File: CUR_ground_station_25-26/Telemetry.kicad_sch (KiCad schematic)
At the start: 0 parts

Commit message: added buncha stuff from flight computer
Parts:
- added C6: 1u, Capacitor_SMD:C_0603_1608Metric, symbol Device:C_Small
- added C8, C9: C_Small, Capacitor_SMD:C_0603_1608Metric, symbol Device:C_Small
- added J3: Conn_Coaxial_Small, Connector_Coxaial_RFSOLUTIONS_CON-SMA-EDGE-S:Conn_Coaxial_RFSOLUTIONS_CON-SMA-EDGE-S, symbol Connector:Conn_Coaxial_Small
- added R23: 10k, Resistor_SMD:R_0603_1608Metric, symbol Device:R_Small_US
- added R24, R25: 0, Resistor_SMD:R_0603_1608Metric, symbol Device:R_Small_US
- added TP1, TP10, TP11, TP2, TP3, TP4, TP5, TP6, TP7, TP8, TP9: TestPoint_Small, TestPoint_KOASpeer:TestPoint_Chip_RCUCTE_0603, symbol Connector:TestPoint_Small
- added U5: E22-400MM_22S, EBYTE_LoRa:EBYTE_LoRA_E22-400MM22S, symbol EBYTE_LoRa:EBYTE_LoRa_E22-400MM22S
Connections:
- new net: C9.1, J3.1 (In), R25.1
- new net: C8.1, R25.2, U5.6 (ANT)
- new net +3V3: C6.1, R23.1, U5.1 (VCC)
- new net GND: C6.2, C8.2, C9.2, J3.2 (Ext), U5.16 (GND), U5.2 (GND), U5.7 (GND)
- new net RF_BUSY: TP3.1, U5.11 (BUSY)
- new net RF_IO1: TP9.1, U5.18 (DIO1)
- new net RF_IO2: R24.2, TP10.1, U5.19 (DIO2)
- new net RF_IO3: TP11.1, U5.20 (DIO3)
- new net RF_MISO: TP7.1, U5.12 (MISO)
- new net RF_MOSI: TP1.1, U5.13 (MOSI)
- new net RF_RXEN: TP4.1, U5.10 (RXEN)
- new net RF_SCK: TP2.1, U5.15 (SCK)
- new net RF_TXEN: R24.1, TP5.1, U5.9 (TXEN)
- new net ~{RF_NSS}: R23.2, TP8.1, U5.14 (NSS)
- new net ~{RF_RESET}: TP6.1, U5.3 (NRST)
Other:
- note added: "DIO1 - interrupt DIO2 - tx switch"
- note added: "Just in case something weird is happening here"
- note added: "Pick capacitor values to PI match antenna - leave to test later - do not place in BOM"
- note added: "RF Module"

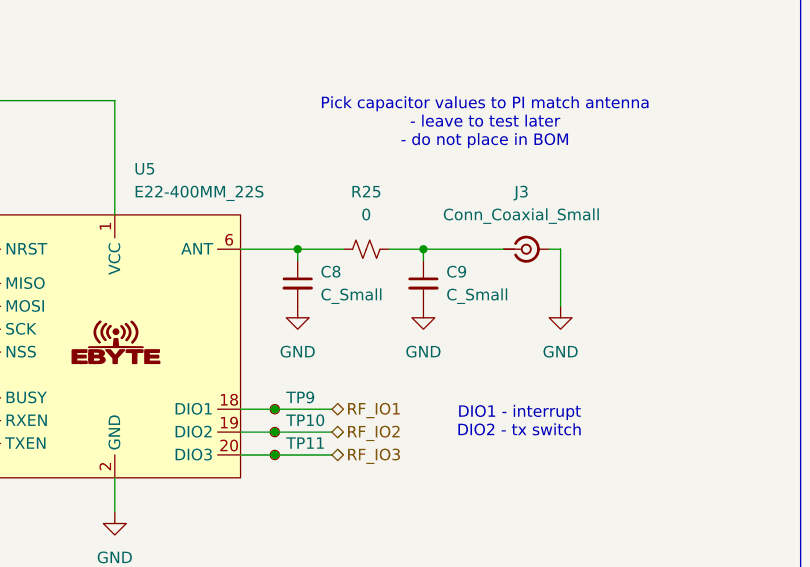
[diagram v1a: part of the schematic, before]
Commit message: DNP the tuning capacitors on the RF trace
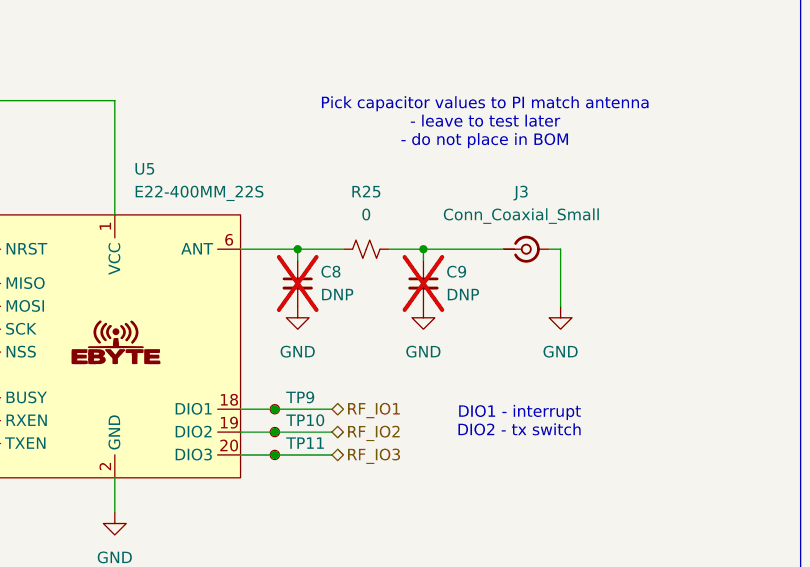
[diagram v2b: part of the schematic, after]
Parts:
- C8, C9: value C_Small -> DNP; now not fitted
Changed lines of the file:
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@@
 		(in_bom yes)
 		(on_board yes)
-		(dnp no)
+		(dnp yes)
 		(fields_autoplaced yes)
 		(property "Reference" "C8"
@@
 			)
 		)
-		(property "Value" "C_Small"
+		(property "Value" "DNP"
 			(at 106.68 60.9662 0)
 			(effects
@@
 		(in_bom yes)
 		(on_board yes)
-		(dnp no)
+		(dnp yes)
 		(fields_autoplaced yes)
 		(property "Reference" "C9"
@@
 			)
 		)
-		(property "Value" "C_Small"
+		(property "Value" "DNP"
 			(at 120.65 60.9662 0)
 			(effects

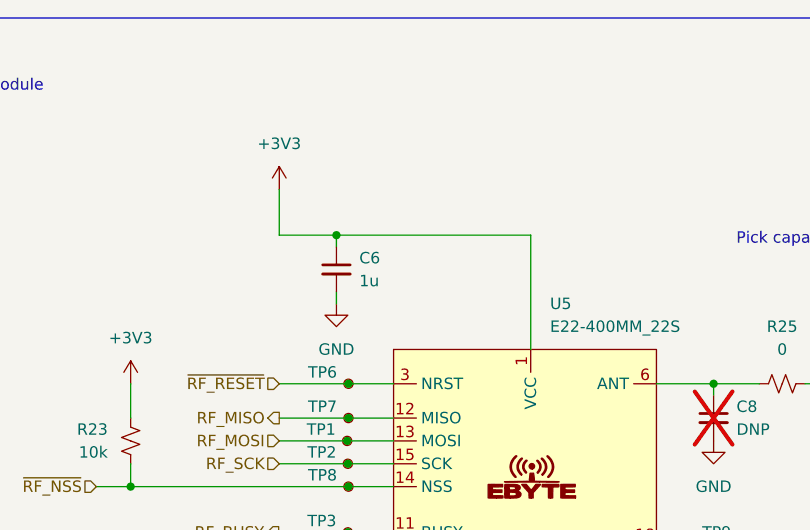
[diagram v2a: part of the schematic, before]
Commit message: Add some required MCU components
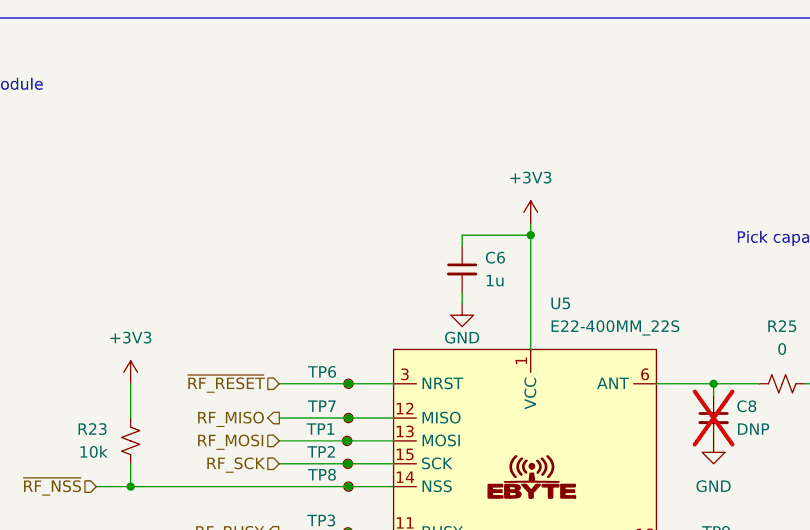
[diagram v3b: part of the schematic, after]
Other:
- moved on the sheet: C6
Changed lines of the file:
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@@
-	)
-	(junction
-		(at 62.23 39.37)
-		(diameter 0)
-		(color 0 0 0 0)
 	)
 	(junction
@@
 	)
 	(junction
+		(at 83.82 39.37)
+		(diameter 0)
+		(color 0 0 0 0)
+	)
+	(junction
 		(at 39.37 67.31)
 		(diameter 0)
@@
 	(wire
 		(pts
-			(xy 62.23 40.64) (xy 62.23 39.37)
+			(xy 76.2 40.64) (xy 76.2 39.37)
 		)
 		(stroke
@@
 	(wire
 		(pts
-			(xy 55.88 34.29) (xy 55.88 39.37)
+			(xy 83.82 38.1) (xy 83.82 39.37)
 		)
 		(stroke
@@
 	(wire
 		(pts
-			(xy 62.23 39.37) (xy 83.82 39.37)
+			(xy 76.2 39.37) (xy 83.82 39.37)
 		)
 		(stroke
@@
 	(wire
 		(pts
-			(xy 62.23 45.72) (xy 62.23 46.99)
+			(xy 76.2 45.72) (xy 76.2 46.99)
 		)
 		(stroke
@@
 		(pts
 			(xy 39.37 55.88) (xy 39.37 59.69)
-		)
-		(stroke
-			(width 0)
-			(type default)
-		)
-	)
-	(wire
-		(pts
-			(xy 55.88 39.37) (xy 62.23 39.37)
 		)
 		(stroke
@@
 	(symbol
 		(lib_id "power:GND")
-		(at 62.23 46.99 0)
+		(at 76.2 46.99 0)
 		(mirror y)
 		(unit 1)
@@
 		(on_board yes)
 		(dnp no)
-		(fields_autoplaced yes)
 		(property "Reference" "#PWR036"
-			(at 62.23 53.34 0)
+			(at 76.2 53.34 0)
 			(effects
 				(font
@@
 		)
 		(property "Value" "GND"
-			(at 62.23 52.07 0)
+			(at 76.2 50.8 0)
 			(effects
 				(font
@@
 		)
 		(property "Footprint" ""
-			(at 62.23 46.99 0)
+			(at 76.2 46.99 0)
 			(effects
 				(font
@@
 		)
 		(property "Datasheet" ""
-			(at 62.23 46.99 0)
+			(at 76.2 46.99 0)
 			(effects
 				(font
@@
 		)
 		(property "Description" "Power symbol creates a global label with name \"GND\" , ground"
-			(at 62.23 46.99 0)
+			(at 76.2 46.99 0)
 			(effects
 				(font
@@
 	(symbol
 		(lib_id "Device:C_Small")
-		(at 62.23 43.18 0)
+		(at 76.2 43.18 0)
 		(mirror y)
 		(unit 1)
@@
 		(fields_autoplaced yes)
 		(property "Reference" "C6"
-			(at 64.77 41.9162 0)
+			(at 78.74 41.9162 0)
 			(effects
 				(font
@@
 		)
 		(property "Value" "1u"
-			(at 64.77 44.4562 0)
+			(at 78.74 44.4562 0)
 			(effects
 				(font
@@
 		)
 		(property "Footprint" "Capacitor_SMD:C_0603_1608Metric"
-			(at 62.23 43.18 0)
+			(at 76.2 43.18 0)
 			(effects
 				(font
@@
 		)
 		(property "Datasheet" "~"
-			(at 62.23 43.18 0)
+			(at 76.2 43.18 0)
 			(effects
 				(font
@@
 		)
 		(property "Description" "Unpolarized capacitor, small symbol"
-			(at 62.23 43.18 0)
+			(at 76.2 43.18 0)
 			(effects
 				(font
@@
 	(symbol
 		(lib_id "power:+3V3")
-		(at 55.88 34.29 0)
+		(at 83.82 38.1 0)
 		(unit 1)
 		(exclude_from_sim no)
@@
 		(fields_autoplaced yes)
 		(property "Reference" "#PWR035"
-			(at 55.88 38.1 0)
+			(at 83.82 41.91 0)
 			(effects
 				(font
@@
 		)
 		(property "Value" "+3V3"
-			(at 55.88 29.21 0)
+			(at 83.82 33.02 0)
 			(effects
 				(font
@@
 		)
 		(property "Footprint" ""
-			(at 55.88 34.29 0)
+			(at 83.82 38.1 0)
 			(effects
 				(font
@@
 		)
 		(property "Datasheet" ""
-			(at 55.88 34.29 0)
+			(at 83.82 38.1 0)
 			(effects
 				(font
@@
 		)
 		(property "Description" "Power symbol creates a global label with name \"+3V3\""
-			(at 55.88 34.29 0)
-			(effects
-				(font
+			(at 83.82 38.1 0)
+			(effects
+				(font

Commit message: added more footprints
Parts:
- J3: footprint Connector_Coxaial_RFSOLUTIONS_CON-SMA-EDGE-S:Conn_Coaxial_RFSOLUTIONS_CON-SMA-EDGE-S -> Conn_Coaxial_RFSOLUTIONS_CON-SMA-EDGE-S:Conn_Coaxial_RFSOLUTIONS_CON-SMA-EDGE-S
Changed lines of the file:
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@@
 			)
 		)
-		(property "Footprint" "Connector_Coxaial_RFSOLUTIONS_CON-SMA-EDGE-S:Conn_Coaxial_RFSOLUTIONS_CON-SMA-EDGE-S"
+		(property "Footprint" "Conn_Coaxial_RFSOLUTIONS_CON-SMA-EDGE-S:Conn_Coaxial_RFSOLUTIONS_CON-SMA-EDGE-S"
 			(at 129.54 55.88 0)
 			(effects

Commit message: BOM optimization
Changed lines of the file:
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@@
 		(lib_id "Device:R_Small_US")
 		(at 62.23 82.55 0)
+		(mirror y)
 		(unit 1)
 		(exclude_from_sim no)
@@
 		(dnp no)
 		(property "Reference" "R24"
-			(at 64.7429 81.2799 0)
+			(at 59.7171 81.2799 0)
 			(effects
 				(font
@@
 		)
 		(property "Value" "0"
-			(at 64.7429 85.0899 0)
+			(at 59.7171 85.0899 0)
 			(effects
 				(font

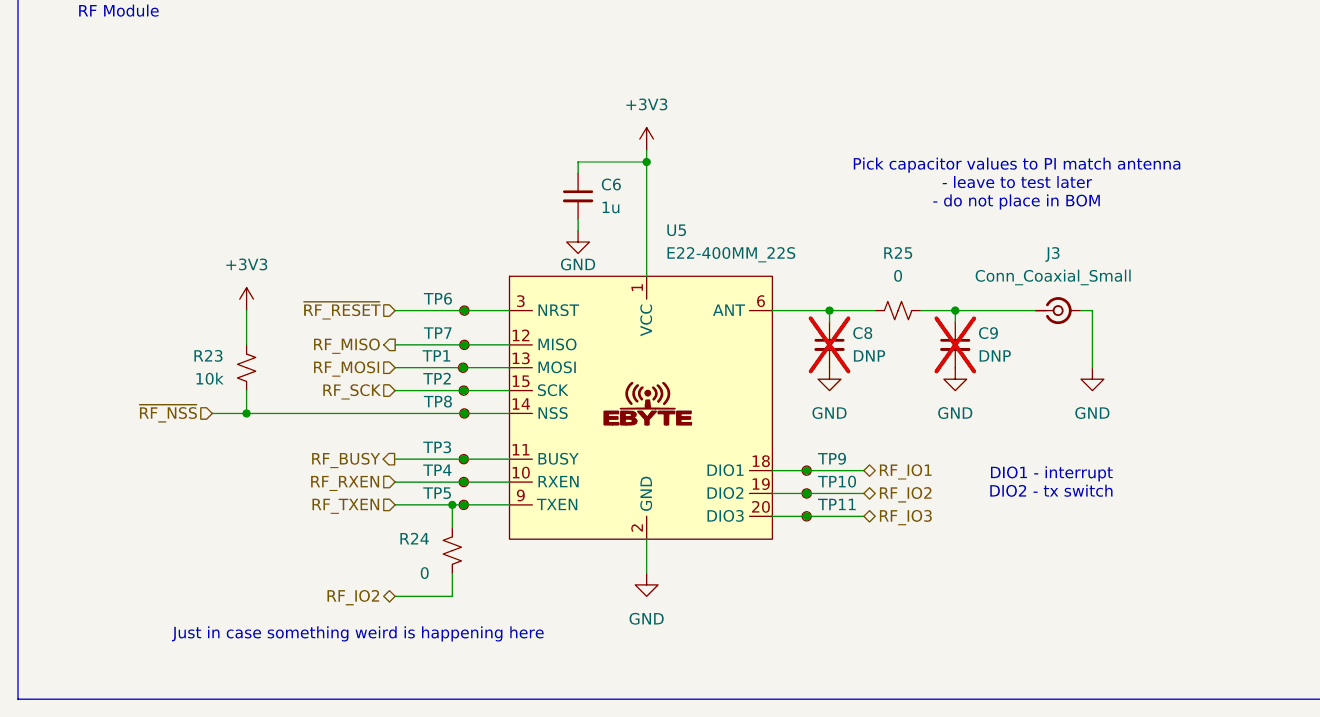
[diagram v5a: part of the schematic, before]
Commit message: Fix library issues in board update
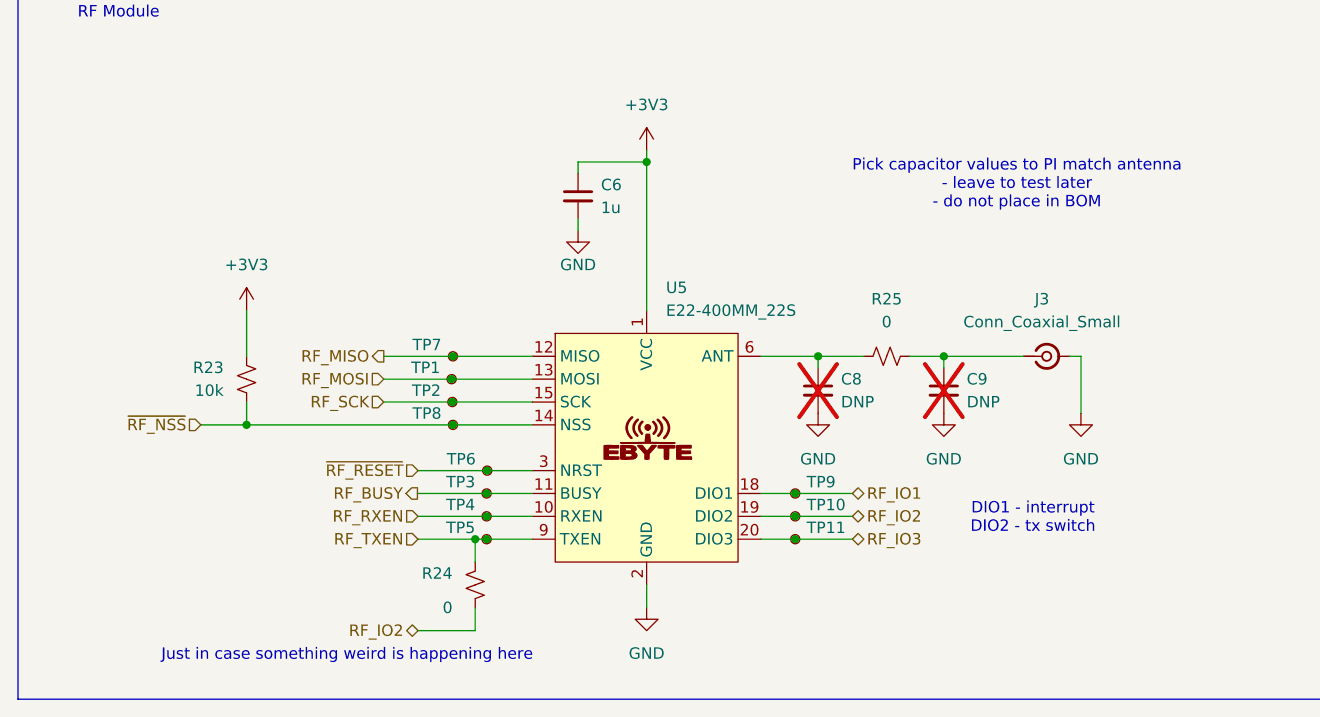
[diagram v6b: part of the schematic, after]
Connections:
- new net: U5.17 (NC), U5.4 (NC), U5.5 (NC), U5.8 (NC)
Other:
- moved on the sheet: C8, C9, J3, R23, R24, R25, TP1, TP10, TP11, TP2, TP3, TP4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

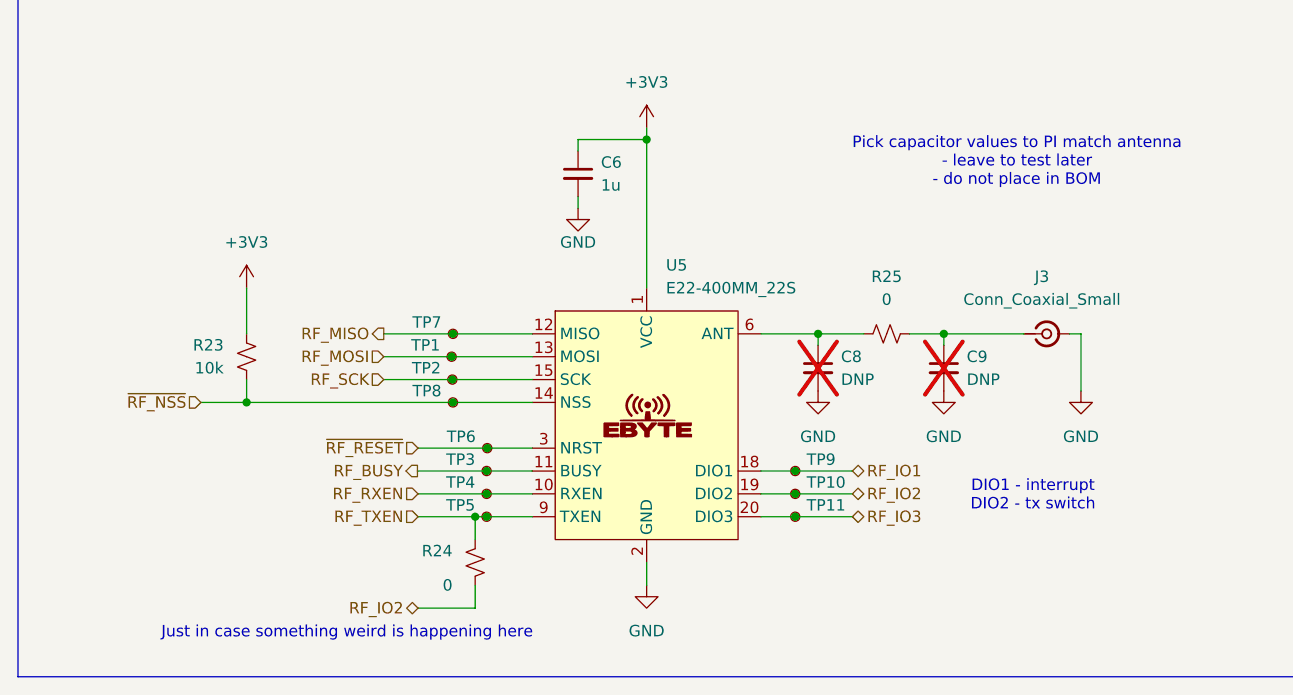
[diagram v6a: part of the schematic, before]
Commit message: Find MPNs again
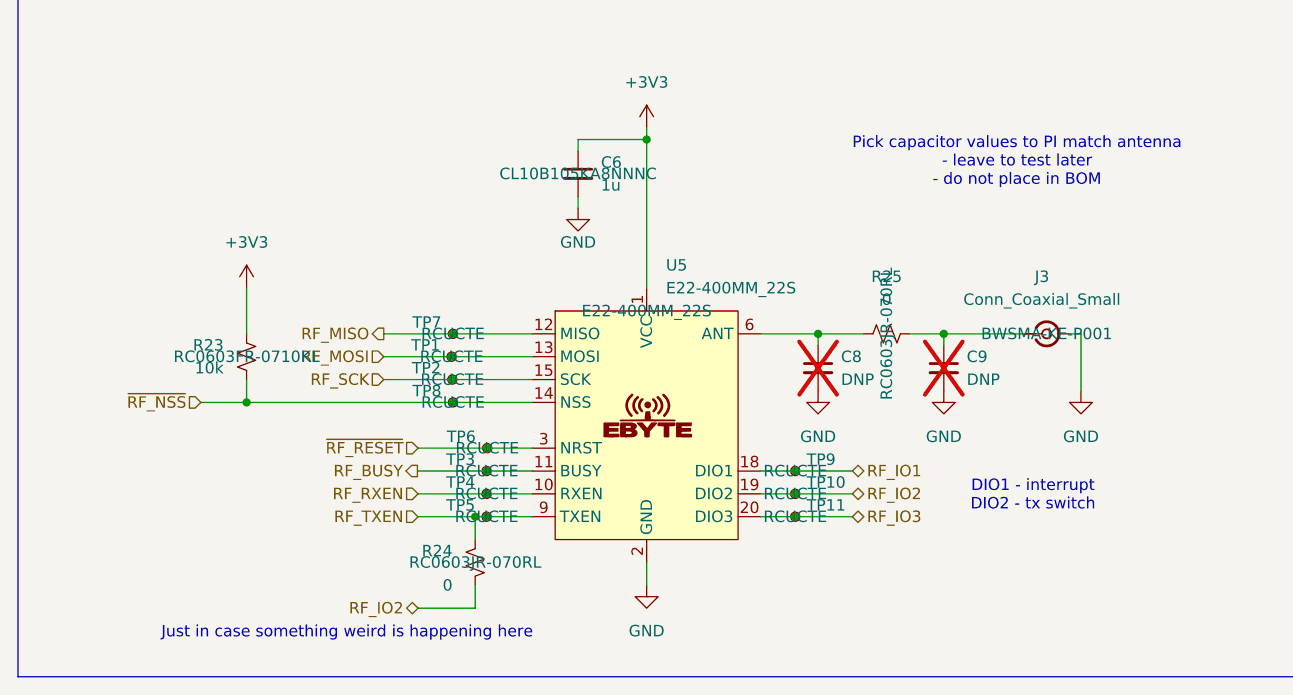
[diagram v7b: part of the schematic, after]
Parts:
- C6: MPN (none) -> CL10B105KA8NNNC
- J3: MPN (none) -> BWSMA-KE-P001
- R23: MPN (none) -> RC0603FR-0710KL
- R24, R25: MPN (none) -> RC0603JR-070RL
- TP1, TP10, TP11, TP2, TP3, TP4, TP5, TP6, TP7, TP8, TP9: MPN (none) -> RCUCTE
- U5: MPN (none) -> E22-400MM_22S
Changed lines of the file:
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@@
+			)
+		)
+		(property "MPN" "RCUCTE"
+			(at 66.1079 73.66 0)
+			(effects
+				(font
+					(size 1.27 1.27)
+				)
 			)
 		)
@@
 			)
 		)
+		(property "MPN" "RCUCTE"
+			(at 62.23 66.04 0)
+			(effects
+				(font
+					(size 1.27 1.27)
+				)
+			)
+		)
 		(pin "1"
 		)
@@
 			)
 		)
+		(property "MPN" "RCUCTE"
+			(at 66.04 76.2 0)
+			(effects
+				(font
+					(size 1.27 1.27)
+				)
+			)
+		)
 		(pin "1"
 		)
@@
 			)
 		)
+		(property "MPN" " RC0603JR-070RL"
+			(at 64.77 86.36 0)
+			(effects
+				(font
+					(size 1.27 1.27)
+				)
+			)
+		)
 		(pin "1"
 		)
@@
 			)
 		)
+		(property "MPN" "RCUCTE"
+			(at 66.04 81.28 0)
+			(effects
+				(font
+					(size 1.27 1.27)
+				)
+			)
+		)
 		(pin "1"
 		)
@@
 			)
 		)
+		(property "MPN" " RC0603JR-070RL"
+			(at 110.49 60.96 0)
+			(effects
+				(font
+					(size 1.27 1.27)
+				)
+			)
+		)
 		(pin "1"
 		)
@@
 			)
 		)
+		(property "MPN" "RC0603FR-0710KL"
+			(at 39.37 63.5 0)
+			(effects
+				(font
+					(size 1.27 1.27)
+				)
+			)
+		)
 		(pin "1"
 		)
@@
 			)
 		)
+		(property "MPN" "RCUCTE"
+			(at 66.04 78.74 0)
+			(effects
+				(font
+					(size 1.27 1.27)
+				)
+			)
+		)
 		(pin "1"
 		)
@@
 				)
 				(hide yes)
+			)
+		)
+		(property "MPN" "CL10B105KA8NNNC"
+			(at 76.2 43.18 0)
+			(effects
+				(font
+					(size 1.27 1.27)
+				)
 			)
 		)
@@
 			)
 		)
+		(property "MPN" "RCUCTE"
+			(at 100.33 78.74 0)
+			(effects
+				(font
+					(size 1.27 1.27)
+				)
+			)
+		)
 		(pin "1"
 		)
@@
 				)
 				(hide yes)
+			)
+		)
+		(property "MPN" "RCUCTE"
+			(at 100.33 81.28 0)
+			(effects
+				(font
+					(size 1.27 1.27)
+				)
 			)
 		)
@@
 			)
 		)
+		(property "MPN" "E22-400MM_22S"
+			(at 83.82 58.42 0)
+			(effects
+				(font
+					(size 1.27 1.27)
+				)
+			)
+		)
 		(pin "10"
 		)
@@
 			)
 		)
+		(property "MPN" "RCUCTE"
+			(at 62.2979 60.96 0)
+			(effects
+				(font
+					(size 1.27 1.27)
+				)
+			)
+		)
 		(pin "1"
 		)
@@
 			)
 		)
+		(property "MPN" "RCUCTE"
+			(at 62.153 63.5 0)
+			(effects
+				(font
+					(size 1.27 1.27)
+				)
+			)
+		)
 		(pin "1"
 		)
@@
 			)
 		)
+		(property "MPN" "BWSMA-KE-P001"
+			(at 128.27 60.96 0)
+			(effects
+				(font
+					(size 1.27 1.27)
+				)
+			)
+		)
 		(pin "1"
 		)
@@
 			)
 		)
+		(property "MPN" "RCUCTE"
+			(at 100.33 76.2 0)
+			(effects
+				(font
+					(size 1.27 1.27)
+				)
+			)
+		)
 		(pin "1"
 		)
@@
 			)
 		)
+		(property "MPN" "RCUCTE"
+			(at 62.2979 68.58 0)
+			(effects
+				(font
+					(size 1.27 1.27)
+				)
+			)
+		)
